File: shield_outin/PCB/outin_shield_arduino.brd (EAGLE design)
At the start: 68.6 x 53.3 mm, 33 parts, among them SW1 POWER, SW2 I2C_PWR, SW4 RESET

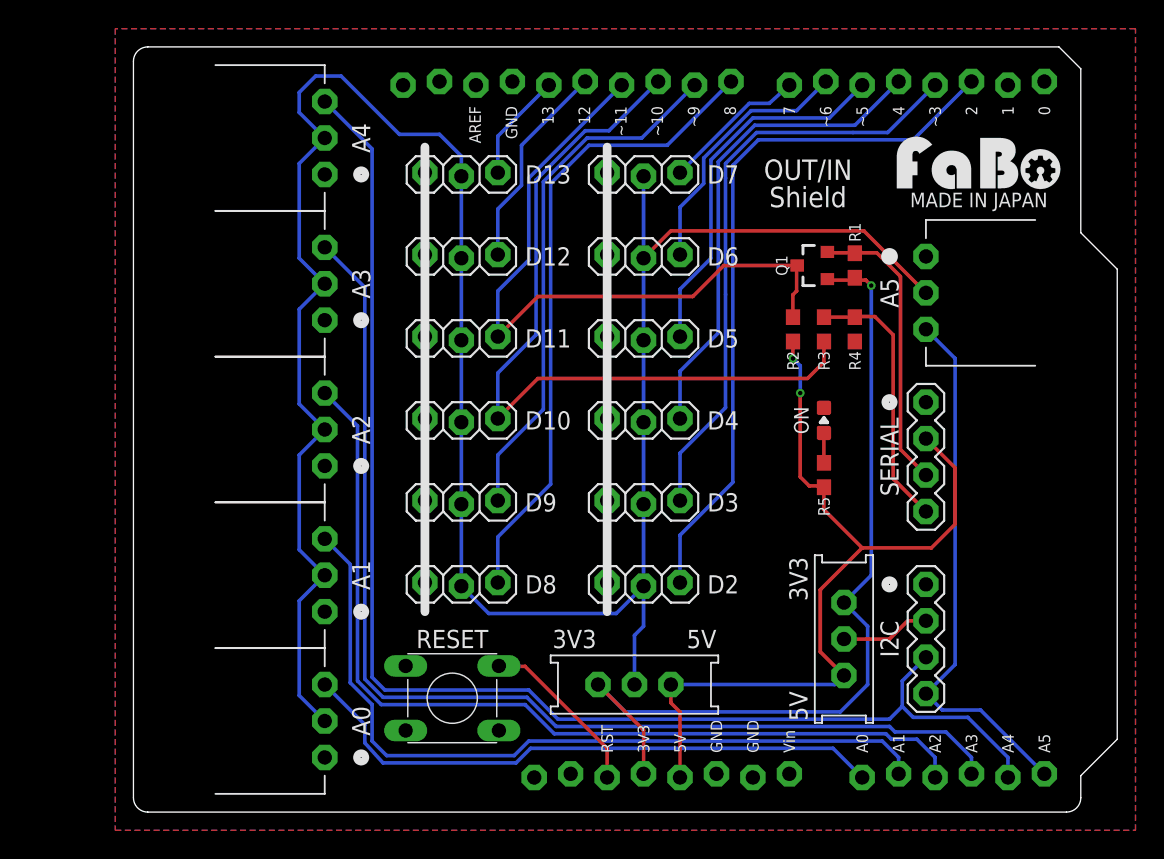
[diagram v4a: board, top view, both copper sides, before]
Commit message: change outin_shield_arduino   Mega I2C support
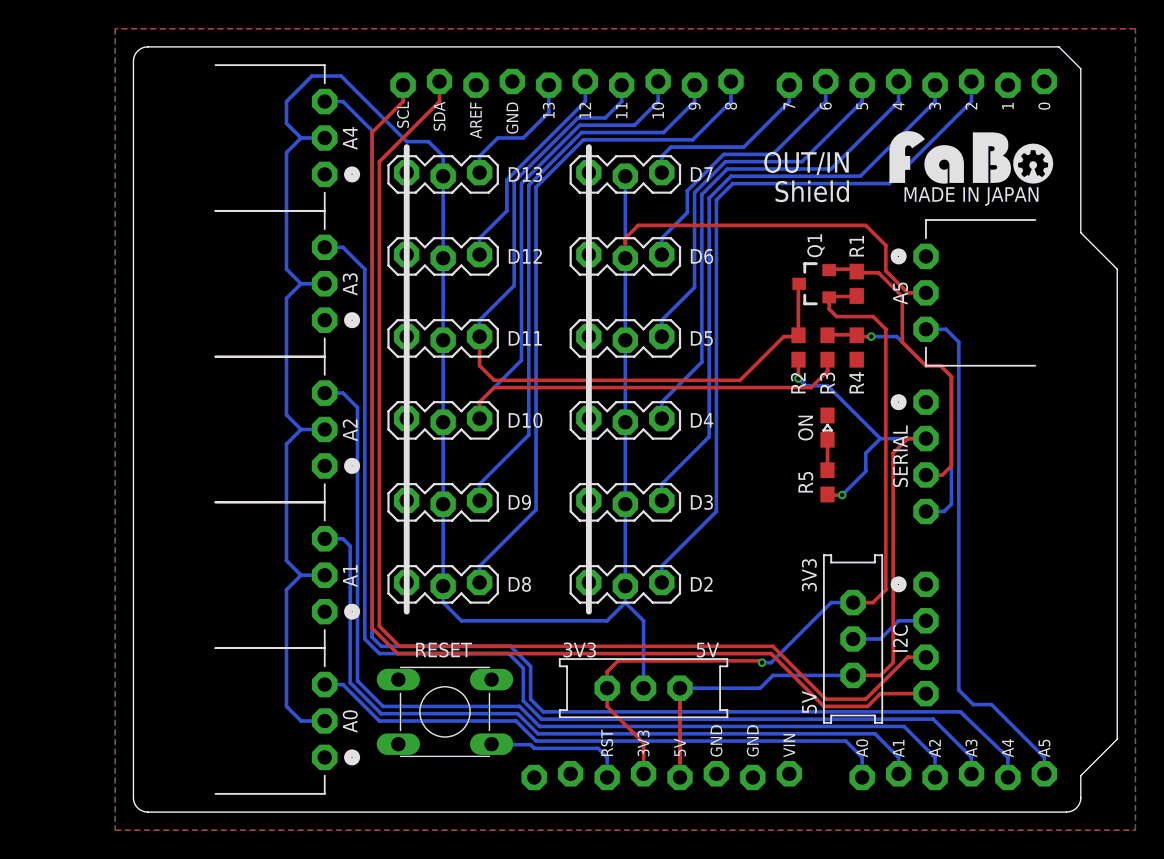
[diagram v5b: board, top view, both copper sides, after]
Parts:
- removed OUT10, OUT11, OUT12, OUT13, OUT2, OUT3, OUT4, OUT5, OUT6, OUT7, OUT8, OUT9: (no value), Gclue:1X3-SNEAKY-BRICK
- removed SW4: RESET, Gclue:DTS_6_V
- removed U$2: (no value), Gclue:LOGO_OSHW_T_M_BOTTOM
- removed U$5: (no value), FaBo:LOGO_FABO_M
- added D10, D11, D12, D13, D2, D3, D4, D5, D6, D7, D8, D9: (no value), FaBo-Template:FABO_BRICK_3PIN_HEADER
- added SW3: RESET, FaBo-etc:DTS_6_V
- added U$21: (no value), FaBo-etc:LOGO_FABO_M
- added U$22: (no value), FaBo-etc:LOGO_OSHW_T_M_BOTTOM
- A0, A1, A2, A3, A4, A5: device Gclue:BRICK_3PIN_CONNECTOR -> FaBo-Template:FABO_BRICK_3PIN_CONNECTOR
- ON: device Gclue:EIA0603-LED -> FaBo-etc:EIA0603-LED
- Q1: device Gclue:SOT23-3 -> FaBo-etc:SOT23-3
- R1, R2, R3: device Gclue:EIA0603 -> FaBo-etc:EIA0603
- R4: value 4k7 -> 4.7k; device Gclue:EIA0603 -> FaBo-etc:EIA0603
- R5: value 220 -> 1k; device Gclue:EIA0603 -> FaBo-etc:EIA0603
- SW1: value POWER -> PIN_PWR; device Gclue:EG1218 -> FaBo-etc:EG1218
- SW2: device Gclue:EG1218 -> FaBo-etc:EG1218
- moved R2 1.33 mm to (46.4, 32.4)
- moved R3 1.30 mm to (48.4, 32.4)
- moved Q1 1.28 mm to (47.5, 36.8)
- moved R1 1.28 mm to (50.4, 36.8)
- moved R4 1.28 mm to (50.4, 32.4)
- moved SW1 0.68 mm to (35.6, 8.64), turned to 0 degrees
- moved SW2 0.63 mm to (50.2, 12.1), turned to 270 degrees
- moved R5 0.57 mm to (48.4, 23.0), turned to 270 degrees
- moved ON 0.57 mm to (48.4, 26.8), turned to 90 degrees
- renumbered I2C_CON to I2C, SERIAL_CON to SERIAL
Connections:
- net SEN0 renamed A0
- net SEN1 renamed A1
- net SEN2 renamed A2
- net SEN3 renamed A3
- removed net N$2: SW4.3, U1.RESET
- removed net N$4: ON.A, R5.2
- removed net OUT0: U1.D0
- removed net OUT1: U1.D1
- removed net OUT10: OUT10.3, R3.2, U1.D10
- removed net OUT11: OUT11.3, Q1.3, R2.1, U1.D11
- removed net OUT12: OUT12.3, U1.D12
- removed net OUT13: OUT13.3, U1.D13
- removed net OUT2: OUT2.3, U1.D2
- removed net OUT3: OUT3.3, U1.D3
- removed net OUT4: OUT4.3, U1.D4
- removed net OUT5: OUT5.3, U1.D5
- removed net OUT6: OUT6.3, U1.D6
- removed net OUT7: OUT7.3, U1.D7
- removed net OUT8: OUT8.3, U1.D8
- removed net OUT9: OUT9.3, U1.D9
- removed net SEN4: A4.IN/OUT, I2C.SDA, U1.A4
- removed net SEN5: A5.IN/OUT, I2C.SCL, U1.A5
- new net A4: A4.IN/OUT, U1.A4
- new net A5: A5.IN/OUT, U1.A5
- new net D10: D10.I/O, R3.2, U1.D10
- new net D11: D11.I/O, Q1.3, R2.1, U1.D11
- new net D12: D12.I/O, U1.D12
- new net D13: D13.I/O, U1.D13
- new net D2: D2.I/O, U1.D2
- new net D3: D3.I/O, U1.D3
- new net D4: D4.I/O, U1.D4
- new net D5: D5.I/O, U1.D5
- new net D6: D6.I/O, U1.D6
- new net D7: D7.I/O, U1.D7
- new net D8: D8.I/O, U1.D8
- new net D9: D9.I/O, U1.D9
- new net LEDANO: ON.A, R5.1
- new net RESET: SW3.4, U1.RESET
- new net SCL: I2C.SCL, U1.SCL
- new net SDA: I2C.SDA, U1.SDA
- net 3V3: now also SW1.1, SW2.1; no longer SW1.3, SW2.3
- net 5V: now also R5.2, SW1.3, SW2.3; no longer R5.1, SW1.1, SW2.1
- net GND: now also D10.GND, D11.GND, D12.GND, D13.GND, D2.GND, D3.GND, D4.GND, D5.GND, D6.GND, D7.GND, D8.GND, D9.GND, SW3.1; no longer OUT10.1, OUT11.1, OUT12.1, OUT13.1, OUT2.1, OUT3.1, OUT4.1, OUT5.1, OUT6.1, OUT7.1, OUT8.1, OUT9.1, SW4.2
- net VCC: now also D10.VCC, D11.VCC, D12.VCC, D13.VCC, D2.VCC, D3.VCC, D4.VCC, D5.VCC, D6.VCC, D7.VCC, D8.VCC, D9.VCC; no longer OUT10.2, OUT11.2, OUT12.2, OUT13.2, OUT2.2, OUT3.2, OUT4.2, OUT5.2, OUT6.2, OUT7.2, OUT8.2, OUT9.2
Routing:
- net SEN4: track 94.4 -> 0.00 mm
- net A4: track 0.00 -> 89.9 mm
- net SDA: track 0.00 -> 81.1 mm
- net SCL: track 0.00 -> 80.0 mm
- net D10: track 0.00 -> 58.0 mm
- net OUT10: track 54.9 -> 0.00 mm
- net D11: track 0.00 -> 52.3 mm
- net D2: track 0.00 -> 50.3 mm
- net OUT2: track 49.7 -> 0.00 mm
- net OUT11: track 47.7 -> 0.00 mm
- net D8: track 0.00 -> 46.6 mm
- net OUT8: track 44.9 -> 0.00 mm
- net D3: track 0.00 -> 42.1 mm
- net OUT3: track 41.7 -> 0.00 mm
- net D9: track 0.00 -> 38.5 mm
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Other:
- board text added: "10"
- board text added: "11"
- board text added: "3"
- board text added: "5"
- board text added: "6"
- board text added: "9"
- board text added: "Rev. 1.0.1"
- board text added: "SCL"
- board text added: "SDA"
- board text added: "VIN"
- board text removed: "D10"
- board text removed: "D11"
- board text removed: "D12"
- board text removed: "D13"
- board text removed: "D2"
- board text removed: "D3"
- board text removed: "D4"
- board text removed: "D5"
- board text removed: "D6"
- board text removed: "D7"
- board text removed: "D8"
- board text removed: "D9"
- board text removed: "I2C"
- board text removed: "Rev.1.0.0"
- board text removed: "SERIAL"
- board text removed: "Vin"
- board text removed: "~10"
- board text removed: "~11"
- board text removed: "~3"
- board text removed: "~5"
- board text removed: "~6"
- board text removed: "~9"
